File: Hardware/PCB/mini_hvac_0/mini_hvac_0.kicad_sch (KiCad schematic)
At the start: 25 parts, among them J1 Conn_01x03_Pin, J10 Conn_01x03_Pin, J11 Conn_01x03_Pin, J12 Conn_01x03_Pin, J13 Conn_01x03_Pin, J14 Conn_01x04_Pin, J15 Conn_01x04_Socket, J16 Conn_01x02_Pin, J17 Conn_01x04_Pin, J2 Conn_01x03_Pin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

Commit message: feat: add enable/disable compressor
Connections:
- net CD_PS: now also J14.1 (Pin_1); no longer J14.4 (Pin_4)
- net GND: now also J14.4 (Pin_4); no longer J14.1 (Pin_1), J14.2 (Pin_2)
- net at C1.1, R2.2: now also J14.2 (Pin_2); no longer J14.3 (Pin_3)
- net CD_EN: now reaches A1.10 (D7)
- net CD_EN: now also J14.3 (Pin_3)
- no-connect marks 11 -> 10
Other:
- moved on the sheet: C1, R2

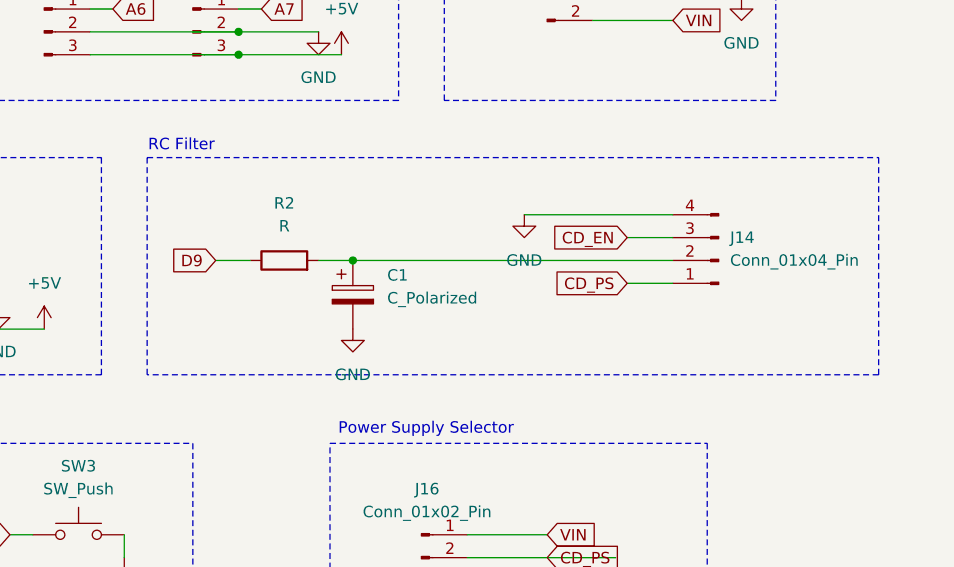
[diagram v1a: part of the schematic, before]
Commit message: footprint changes and schematic clean up
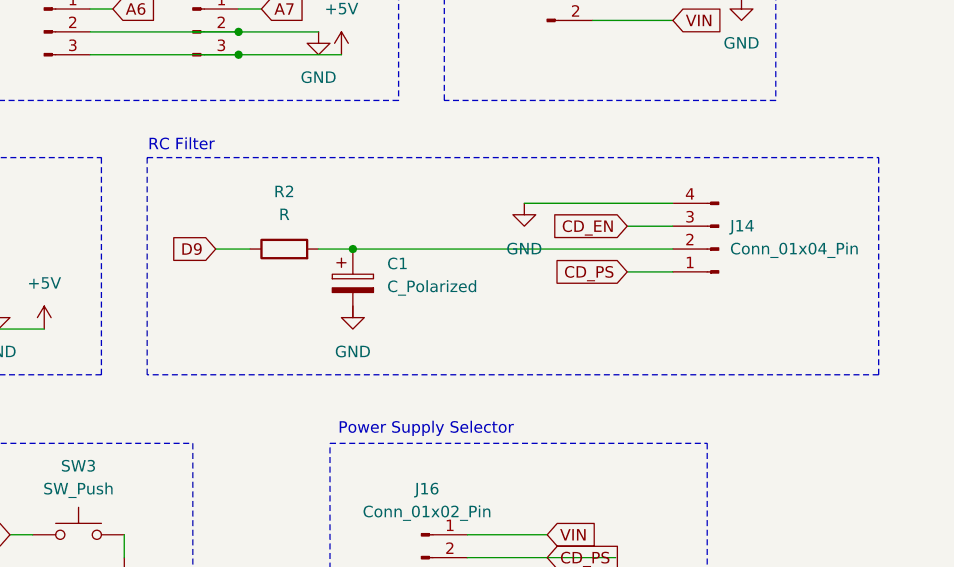
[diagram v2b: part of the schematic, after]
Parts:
- J20: footprint Connector_PinSocket_2.54mm:PinSocket_1x06_P2.54mm_Vertical -> Connector_PinSocket_2.54mm:PinSocket_1x06_P2.54mm_Horizontal
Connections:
- net GND: no longer C1.2
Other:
- moved on the sheet: C1, J14, R2
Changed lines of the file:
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@@
 	)
 	(junction
-		(at 204.47 95.25)
+		(at 204.47 93.98)
 		(diameter 0)
 		(color 0 0 0 0)
@@
 	(wire
 		(pts
-			(xy 234.95 92.71) (xy 240.03 92.71)
+			(xy 234.95 91.44) (xy 240.03 91.44)
 		)
 		(stroke
@@
 	(wire
 		(pts
-			(xy 234.95 97.79) (xy 240.03 97.79)
+			(xy 234.95 96.52) (xy 240.03 96.52)
 		)
 		(stroke
@@
 	(wire
 		(pts
-			(xy 189.23 95.25) (xy 193.04 95.25)
+			(xy 189.23 93.98) (xy 193.04 93.98)
 		)
 		(stroke
@@
 	(wire
 		(pts
-			(xy 204.47 95.25) (xy 240.03 95.25)
+			(xy 204.47 93.98) (xy 240.03 93.98)
 		)
 		(stroke
@@
 	(wire
 		(pts
-			(xy 200.66 95.25) (xy 204.47 95.25)
+			(xy 200.66 93.98) (xy 204.47 93.98)
 		)
 		(stroke
@@
 	(wire
 		(pts
-			(xy 223.52 90.17) (xy 240.03 90.17)
+			(xy 223.52 88.9) (xy 240.03 88.9)
 		)
 		(stroke
@@
 	(global_label "CD_EN"
 		(shape input)
-		(at 234.95 92.71 180)
+		(at 234.95 91.44 180)
 		(fields_autoplaced yes)
 		(effects
@@
 		)
 		(property "Intersheetrefs" "${INTERSHEET_REFS}"
-			(at 225.9777 92.71 0)
+			(at 225.9777 91.44 0)
 			(effects
 				(font
@@
 	(global_label "D9"
 		(shape input)
-		(at 189.23 95.25 180)
+		(at 189.23 93.98 180)
 		(fields_autoplaced yes)
 		(effects
@@
 		)
 		(property "Intersheetrefs" "${INTERSHEET_REFS}"
-			(at 183.7653 95.25 0)
+			(at 183.7653 93.98 0)
 			(effects
 				(font
@@
 	(global_label "CD_PS"
 		(shape input)
-		(at 234.95 97.79 180)
+		(at 234.95 96.52 180)
 		(fields_autoplaced yes)
 		(effects
@@
 		)
 		(property "Intersheetrefs" "${INTERSHEET_REFS}"
-			(at 225.9777 97.79 0)
+			(at 225.9777 96.52 0)
 			(effects
 				(font
@@
 		(length 2.54)
 		(shape dot)
-		(at 215.9 95.25 0)
+		(at 215.9 93.98 0)
 		(fields_autoplaced yes)
 		(effects
@@
 		)
 		(property "Netclass" "Power"
-			(at 216.5985 92.71 0)
+			(at 216.5985 91.44 0)
 			(effects
 				(font
@@
 		)
 		(property "Component Class" ""
-			(at -82.55 1.27 0)
+			(at -82.55 0 0)
 			(effects
 				(font
@@
 	(symbol
 		(lib_id "Device:C_Polarized")
-		(at 204.47 99.06 0)
+		(at 204.47 97.79 0)
 		(unit 1)
 		(exclude_from_sim no)
@@
 		(fields_autoplaced yes)
 		(property "Reference" "C1"
-			(at 208.28 96.9009 0)
+			(at 208.28 95.6309 0)
 			(effects
 				(font
@@
 		)
 		(property "Value" "C_Polarized"
-			(at 208.28 99.4409 0)
+			(at 208.28 98.1709 0)
 			(effects
 				(font
@@
 		)
 		(property "Footprint" "Capacitor_THT:CP_Radial_D5.0mm_P2.00mm"
-			(at 205.4352 102.87 0)
+			(at 205.4352 101.6 0)
 			(effects
 				(font
@@
 		)
 		(property "Datasheet" "~"
-			(at 204.47 99.06 0)
+			(at 204.47 97.79 0)
 			(effects
 				(font
@@
 		)
 		(property "Description" "Polarized capacitor"
-			(at 204.47 99.06 0)
+			(at 204.47 97.79 0)
 			(effects
 				(font
@@
 	(symbol
 		(lib_id "power:GND")
-		(at 204.47 102.87 0)
+		(at 204.47 100.33 0)
 		(unit 1)
 		(exclude_from_sim no)
@@
 		(fields_autoplaced yes)
 		(property "Reference" "#PWR010"
-			(at 204.47 109.22 0)
+			(at 204.47 106.68 0)
 			(effects
 				(font
@@
 		)
 		(property "Value" "GND"
-			(at 204.47 107.95 0)
+			(at 204.47 105.41 0)
 			(effects
 				(font
@@
 		)
 		(property "Footprint" ""
-			(at 204.47 102.87 0)
+			(at 204.47 100.33 0)
 			(effects
 				(font
@@
 		)
 		(property "Datasheet" ""
-			(at 204.47 102.87 0)
+			(at 204.47 100.33 0)
 			(effects
 				(font
@@
 		)
 		(property "Description" "Power symbol creates a global label with name \"GND\" , ground"
-			(at 204.47 102.87 0)
+			(at 204.47 100.33 0)
 			(effects
 				(font
@@
 			)
 		)
-		(property "Footprint" "Connector_PinSocket_2.54mm:PinSocket_1x06_P2.54mm_Vertical"
+		(property "Footprint" "Connector_PinSocket_2.54mm:PinSocket_1x06_P2.54mm_Horizontal"
 			(at 116.84 165.1 0)
 			(effects
@@
 	(symbol
 		(lib_id "power:GND")
-		(at 223.52 90.17 0)
+		(at 223.52 88.9 0)
 		(unit 1)
 		(exclude_from_sim no)
@@
 		(fields_autoplaced yes)
 		(property "Reference" "#PWR08"
-			(at 223.52 96.52 0)
+			(at 223.52 95.25 0)
 			(effects
 				(font
@@
 		)
 		(property "Value" "GND"
-			(at 223.52 95.25 0)
+			(at 223.52 93.98 0)
 			(effects
 				(font
@@
 		)
 		(property "Footprint" ""
-			(at 223.52 90.17 0)
+			(at 223.52 88.9 0)
 			(effects
 				(font
@@
 		)
 		(property "Datasheet" ""
-			(at 223.52 90.17 0)
+			(at 223.52 88.9 0)
 			(effects
 				(font
@@
 		)
 		(property "Description" "Power symbol creates a global label with name \"GND\" , ground"
-			(at 223.52 90.17 0)
+			(at 223.52 88.9 0)
 			(effects
 				(font
@@
 	(symbol
 		(lib_id "Device:R")
-		(at 196.85 95.25 90)
+		(at 196.85 93.98 90)
 		(unit 1)
 		(exclude_from_sim no)
@@
 		(fields_autoplaced yes)
 		(property "Reference" "R2"
-			(at 196.85 88.9 90)
+			(at 196.85 87.63 90)
 			(effects
 				(font
@@
 		)
 		(property "Value" "R"
-			(at 196.85 91.44 90)
+			(at 196.85 90.17 90)
 			(effects
 				(font
@@
 		)
 		(property "Footprint" "Resistor_THT:R_Axial_DIN0207_L6.3mm_D2.5mm_P7.62mm_Horizontal"
-			(at 196.85 97.028 90)
+			(at 196.85 95.758 90)
 			(effects
 				(font
@@
 		)
 		(property "Datasheet" "~"
-			(at 196.85 95.25 0)
+			(at 196.85 93.98 0)
 			(effects
 				(font
@@
 		)
 		(property "Description" "Resistor"
-			(at 196.85 95.25 0)
+			(at 196.85 93.98 0)
 			(effects
 				(font
@@
 	(symbol
 		(lib_id "Connector:Conn_01x04_Pin")
-		(at 245.11 95.25 180)
+		(at 245.11 93.98 180)
 		(unit 1)
 		(exclude_from_sim no)
@@
 		(fields_autoplaced yes)
 		(property "Reference" "J14"
-			(at 246.38 92.7099 0)
+			(at 246.38 91.4399 0)
 			(effects
 				(font
@@
 		)
 		(property "Value" "Conn_01x04_Pin"
-			(at 246.38 95.2499 0)
+			(at 246.38 93.9799 0)
 			(effects
 				(font
@@
 		)
 		(property "Footprint" "Connector_JST:JST_XH_S4B-XH-A_1x04_P2.50mm_Horizontal"
-			(at 245.11 95.25 0)
+			(at 245.11 93.98 0)
 			(effects
 				(font
@@
 		)
 		(property "Datasheet" "~"
-			(at 245.11 95.25 0)
+			(at 245.11 93.98 0)
 			(effects
 				(font
@@
 		)
 		(property "Description" "Generic connector, single row, 01x04, script generated"
-			(at 245.11 95.25 0)
+			(at 245.11 93.98 0)
 			(effects
 				(font

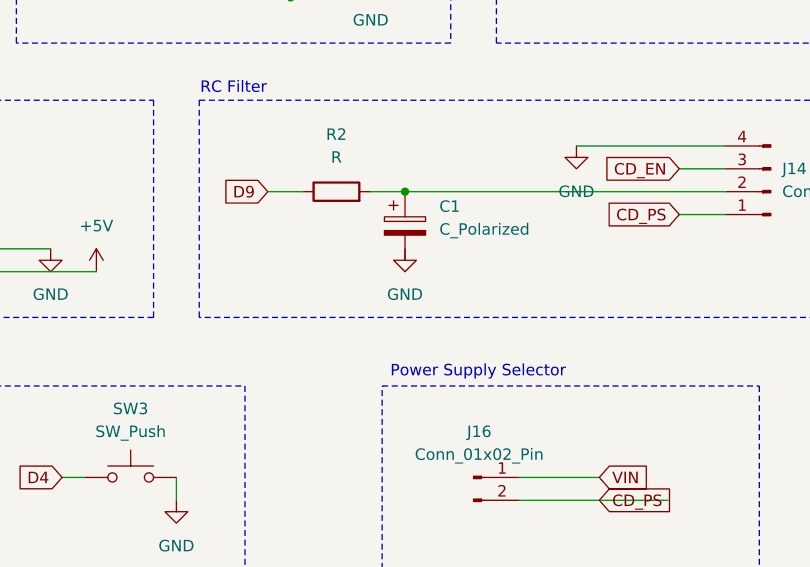
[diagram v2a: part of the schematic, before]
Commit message: new PCB layout
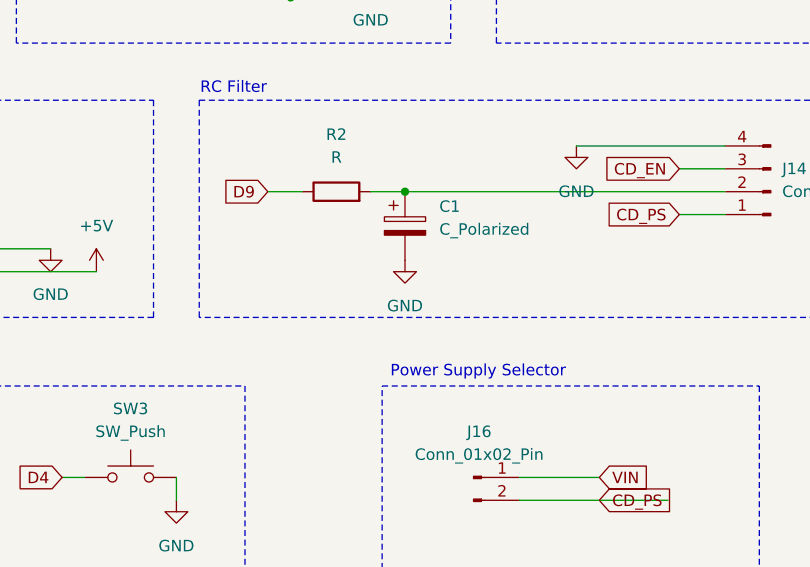
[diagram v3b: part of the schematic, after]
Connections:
- net GND: now also C1.2
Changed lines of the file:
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@@
 	(symbol
 		(lib_id "power:GND")
-		(at 204.47 100.33 0)
+		(at 204.47 101.6 0)
 		(unit 1)
 		(exclude_from_sim no)
@@
 		(fields_autoplaced yes)
 		(property "Reference" "#PWR010"
-			(at 204.47 106.68 0)
+			(at 204.47 107.95 0)
 			(effects
 				(font
@@
 		)
 		(property "Value" "GND"
-			(at 204.47 105.41 0)
+			(at 204.47 106.68 0)
 			(effects
 				(font
@@
 		)
 		(property "Footprint" ""
-			(at 204.47 100.33 0)
+			(at 204.47 101.6 0)
 			(effects
 				(font
@@
 		)
 		(property "Datasheet" ""
-			(at 204.47 100.33 0)
+			(at 204.47 101.6 0)
 			(effects
 				(font
@@
 		)
 		(property "Description" "Power symbol creates a global label with name \"GND\" , ground"
-			(at 204.47 100.33 0)
+			(at 204.47 101.6 0)
 			(effects
 				(font

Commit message: final pcb, shrinked
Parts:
- J14: footprint Connector_JST:JST_XH_S4B-XH-A_1x04_P2.50mm_Horizontal -> Connector_JST:JST_XH_B4B-XH-A_1x04_P2.50mm_Vertical
- J20: footprint Connector_PinSocket_2.54mm:PinSocket_1x06_P2.54mm_Horizontal -> Connector_PinSocket_2.54mm:PinSocket_1x06_P2.54mm_Vertical
- J9: footprint Connector_JST:JST_XH_S2B-XH-A_1x02_P2.50mm_Horizontal -> Connector_JST:JST_XH_B2B-XH-A_1x02_P2.50mm_Vertical
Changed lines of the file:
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@@
 			)
 		)
-		(property "Footprint" "Connector_PinSocket_2.54mm:PinSocket_1x06_P2.54mm_Horizontal"
+		(property "Footprint" "Connector_PinSocket_2.54mm:PinSocket_1x06_P2.54mm_Vertical"
 			(at 116.84 165.1 0)
 			(effects
@@
 			)
 		)
-		(property "Footprint" "Connector_JST:JST_XH_S2B-XH-A_1x02_P2.50mm_Horizontal"
+		(property "Footprint" "Connector_JST:JST_XH_B2B-XH-A_1x02_P2.50mm_Vertical"
 			(at 226.06 66.04 0)
 			(effects
@@
 			)
 		)
-		(property "Footprint" "Connector_JST:JST_XH_S4B-XH-A_1x04_P2.50mm_Horizontal"
+		(property "Footprint" "Connector_JST:JST_XH_B4B-XH-A_1x04_P2.50mm_Vertical"
 			(at 245.11 93.98 0)
 			(effects
